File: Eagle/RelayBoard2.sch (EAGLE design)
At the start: 4 parts, among them K1 4052, X2 MKDSN1,5/3-5,08, X3 MKDSN1,5/3-5,08

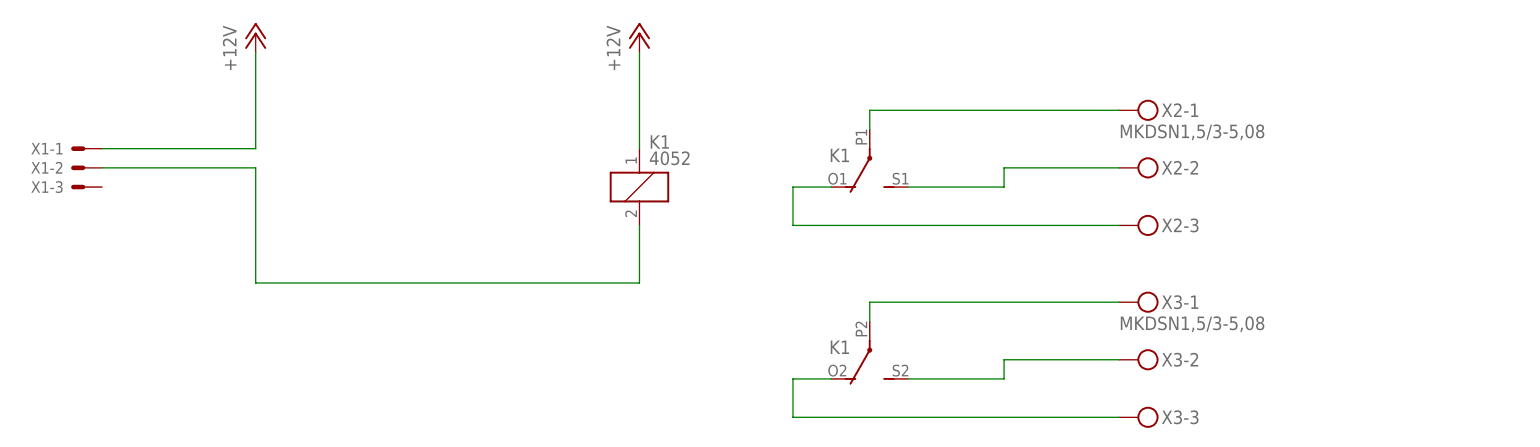
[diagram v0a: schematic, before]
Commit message: - correction to RelayBoard2 - added schematic for PowerSupply (no board so far)
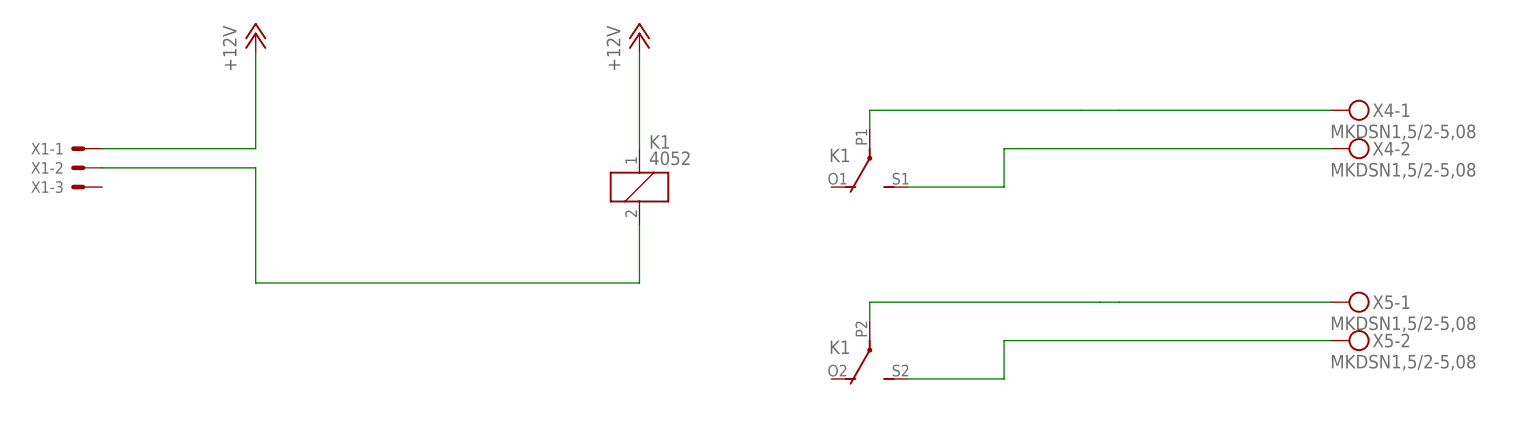
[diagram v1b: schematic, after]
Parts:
- removed X2, X3: MKDSN1,5/3-5,08, con-phoenix-508:MKDSN1,5/3-5,08
- added X4, X5: MKDSN1,5/2-5,08, con-phoenix-508:MKDSN1,5/2-5,08
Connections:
- removed net N$1: K13.O, X3-3.KL
- removed net N$5: K12.O, X2-3.KL
- net N$3: now also X5-1.KL; no longer X3-1.KL
- net N$4: now also X5-2.KL; no longer X3-2.KL
- net N$6: now also X4-2.KL; no longer X2-2.KL
- net N$7: now also X4-1.KL; no longer X2-1.KL
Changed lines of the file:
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@@
 <layer number="91" name="Nets" color="2" fill="1" visible="yes" active="yes"/>
 <layer number="92" name="Busses" color="1" fill="1" visible="yes" active="yes"/>
-<layer number="93" name="Pins" color="2" fill="1" visible="no" active="yes"/>
+<layer number="93" name="Pins" color="2" fill="1" visible="yes" active="yes"/>
 <layer number="94" name="Symbols" color="4" fill="1" visible="yes" active="yes"/>
 <layer number="95" name="Names" color="7" fill="1" visible="yes" active="yes"/>
@@
 <part name="X1" library="con-molex" deviceset="KK-156-3" device=""/>
 <part name="K1" library="relay" deviceset="4052" device=""/>
-<part name="X2" library="con-phoenix-508" deviceset="MKDSN1,5/3-5,08" device=""/>
-<part name="X3" library="con-phoenix-508" deviceset="MKDSN1,5/3-5,08" device=""/>
 <part name="P+1" library="supply1" deviceset="+12V" device=""/>
 <part name="P+2" library="supply1" deviceset="+12V" device=""/>
+<part name="X4" library="con-phoenix-508" deviceset="MKDSN1,5/2-5,08" device=""/>
+<part name="X5" library="con-phoenix-508" deviceset="MKDSN1,5/2-5,08" device=""/>
 </parts>
 <sheets>
@@
 <instance part="K1" gate="2" x="119.38" y="152.4" rot="R180"/>
 <instance part="K1" gate="3" x="119.38" y="127" rot="R180"/>
-<instance part="X2" gate="-1" x="154.94" y="157.48"/>
-<instance part="X2" gate="-2" x="154.94" y="149.86"/>
-<instance part="X2" gate="-3" x="154.94" y="142.24"/>
-<instance part="X3" gate="-1" x="154.94" y="132.08"/>
-<instance part="X3" gate="-2" x="154.94" y="124.46"/>
-<instance part="X3" gate="-3" x="154.94" y="116.84"/>
 <instance part="P+1" gate="1" x="38.1" y="167.64"/>
 <instance part="P+2" gate="1" x="88.9" y="167.64"/>
+<instance part="X4" gate="-1" x="182.88" y="157.48"/>
+<instance part="X4" gate="-2" x="182.88" y="152.4"/>
+<instance part="X5" gate="-1" x="182.88" y="132.08"/>
+<instance part="X5" gate="-2" x="182.88" y="127"/>
 </instances>
 <busses>
@@
 <net name="N$3" class="0">
 <segment>
-<pinref part="X3" gate="-1" pin="KL"/>
-<wire x1="152.4" y1="132.08" x2="119.38" y2="132.08" width="0.1524" layer="91"/>
+<wire x1="152.4" y1="132.08" x2="149.86" y2="132.08" width="0.1524" layer="91"/>
 <pinref part="K1" gate="3" pin="P"/>
+<wire x1="149.86" y1="132.08" x2="119.38" y2="132.08" width="0.1524" layer="91"/>
 <wire x1="119.38" y1="132.08" x2="119.38" y2="129.54" width="0.1524" layer="91"/>
+<pinref part="X5" gate="-1" pin="KL"/>
+<wire x1="152.4" y1="132.08" x2="180.34" y2="132.08" width="0.1524" layer="91"/>
 </segment>
 </net>
@@
 <pinref part="K1" gate="3" pin="S"/>
 <wire x1="124.46" y1="121.92" x2="137.16" y2="121.92" width="0.1524" layer="91"/>
-<wire x1="137.16" y1="121.92" x2="137.16" y2="124.46" width="0.1524" layer="91"/>
-<pinref part="X3" gate="-2" pin="KL"/>
-<wire x1="137.16" y1="124.46" x2="152.4" y2="124.46" width="0.1524" layer="91"/>
-</segment>
-</net>
-<net name="N$1" class="0">
-<segment>
-<pinref part="X3" gate="-3" pin="KL"/>
-<wire x1="152.4" y1="116.84" x2="109.22" y2="116.84" width="0.1524" layer="91"/>
-<wire x1="109.22" y1="116.84" x2="109.22" y2="121.92" width="0.1524" layer="91"/>
-<pinref part="K1" gate="3" pin="O"/>
-<wire x1="109.22" y1="121.92" x2="114.3" y2="121.92" width="0.1524" layer="91"/>
-</segment>
-</net>
-<net name="N$5" class="0">
-<segment>
-<pinref part="X2" gate="-3" pin="KL"/>
-<wire x1="152.4" y1="142.24" x2="109.22" y2="142.24" width="0.1524" layer="91"/>
-<wire x1="109.22" y1="142.24" x2="109.22" y2="147.32" width="0.1524" layer="91"/>
-<pinref part="K1" gate="2" pin="O"/>
-<wire x1="109.22" y1="147.32" x2="114.3" y2="147.32" width="0.1524" layer="91"/>
+<pinref part="X5" gate="-2" pin="KL"/>
+<wire x1="180.34" y1="127" x2="137.16" y2="127" width="0.1524" layer="91"/>
+<wire x1="137.16" y1="127" x2="137.16" y2="121.92" width="0.1524" layer="91"/>
 </segment>
 </net>
 <net name="N$6" class="0">
 <segment>
-<pinref part="X2" gate="-2" pin="KL"/>
-<wire x1="152.4" y1="149.86" x2="137.16" y2="149.86" width="0.1524" layer="91"/>
-<wire x1="137.16" y1="149.86" x2="137.16" y2="147.32" width="0.1524" layer="91"/>
 <pinref part="K1" gate="2" pin="S"/>
 <wire x1="137.16" y1="147.32" x2="124.46" y2="147.32" width="0.1524" layer="91"/>
+<pinref part="X4" gate="-2" pin="KL"/>
+<wire x1="180.34" y1="152.4" x2="137.16" y2="152.4" width="0.1524" layer="91"/>
+<wire x1="137.16" y1="152.4" x2="137.16" y2="147.32" width="0.1524" layer="91"/>
 </segment>
 </net>
 <net name="N$7" class="0">
 <segment>
-<pinref part="X2" gate="-1" pin="KL"/>
 <pinref part="K1" gate="2" pin="P"/>
-<wire x1="152.4" y1="157.48" x2="119.38" y2="157.48" width="0.1524" layer="91"/>
+<wire x1="152.4" y1="157.48" x2="147.32" y2="157.48" width="0.1524" layer="91"/>
+<wire x1="147.32" y1="157.48" x2="119.38" y2="157.48" width="0.1524" layer="91"/>
 <wire x1="119.38" y1="157.48" x2="119.38" y2="154.94" width="0.1524" layer="91"/>
+<pinref part="X4" gate="-1" pin="KL"/>
+<wire x1="180.34" y1="157.48" x2="152.4" y2="157.48" width="0.1524" layer="91"/>
 </segment>
 </net>
